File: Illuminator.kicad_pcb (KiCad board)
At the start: 2 copper layers, 70 x 70 mm, 14 parts, among them J0 Conn_01x03_Male, Q0 BSN20

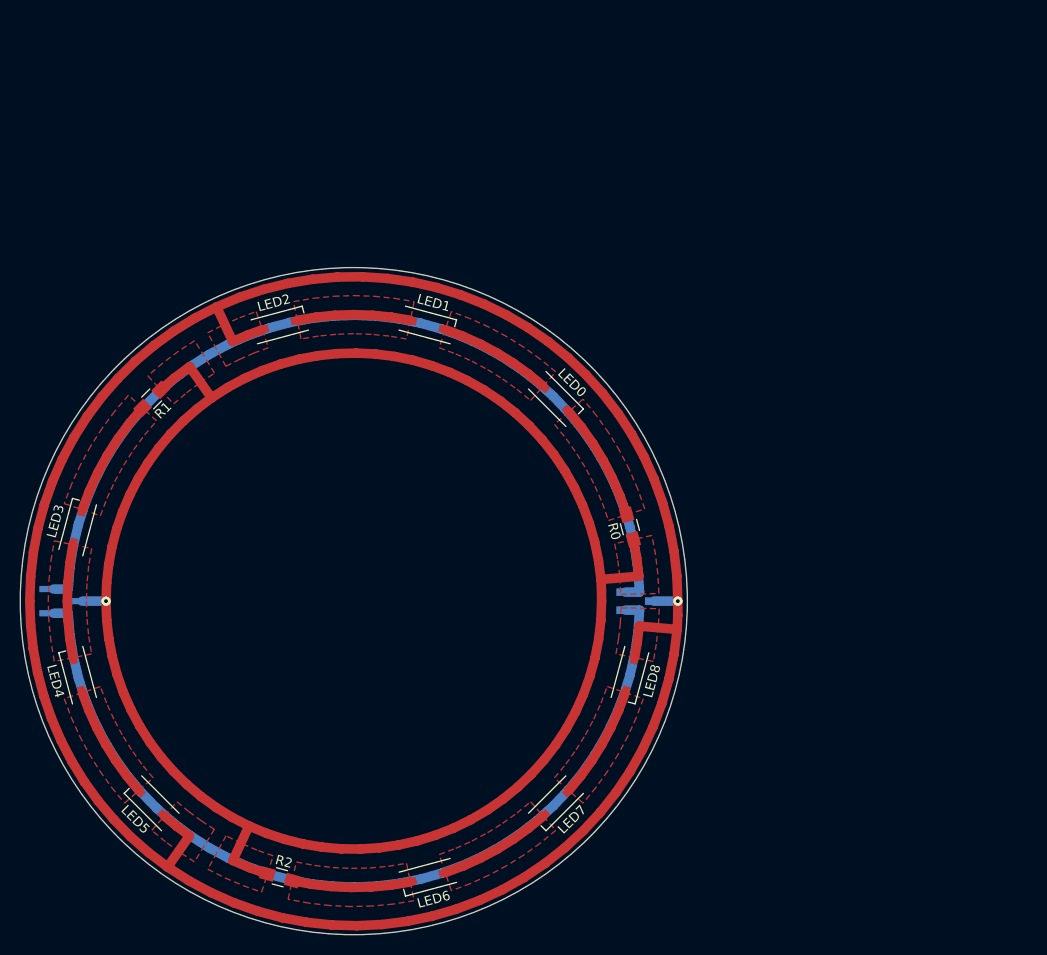
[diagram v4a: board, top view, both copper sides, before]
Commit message: Bugfixes in radial.py and resetting pcb
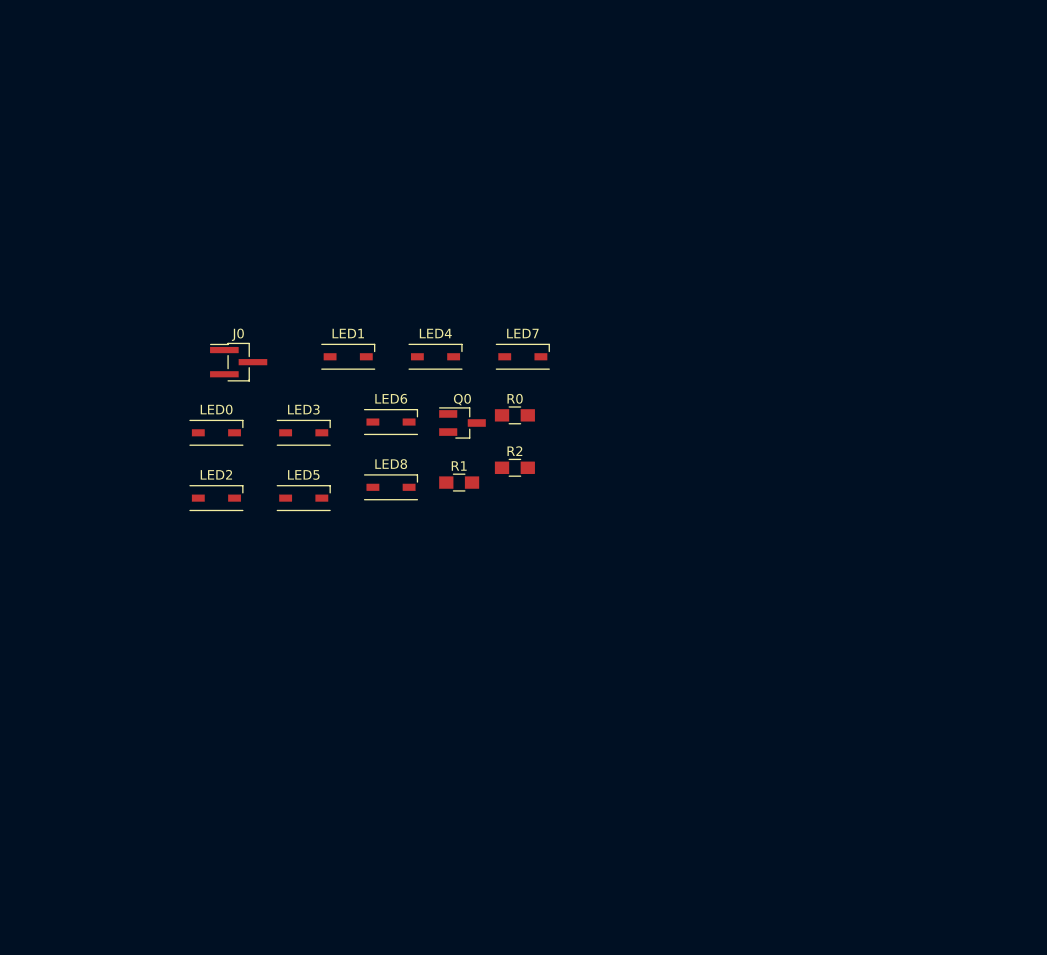
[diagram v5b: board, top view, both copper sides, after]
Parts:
- J0, Q0: moved to F.Cu
- moved LED4 50.3 mm to (108.6, 74.4), turned to 0 degrees
- moved R2 49.5 mm to (116.9, 86.0), turned to 0 degrees
- moved LED6 47.9 mm to (103.9, 81.2), turned to 0 degrees
- moved LED7 47.0 mm to (117.7, 74.4), turned to 0 degrees
- moved LED0 35.8 mm to (85.6, 82.3), turned to 0 degrees
- moved LED5 35.8 mm to (94.7, 89.2), turned to 0 degrees
- moved R1 33.4 mm to (111.1, 87.6), turned to 0 degrees
- moved LED8 31.9 mm to (103.9, 88.1), turned to 0 degrees
- moved J0 30.8 mm to (87.9, 74.9)
- moved Q0 26.4 mm to (111.4, 81.3)
- moved LED3 25.7 mm to (94.7, 82.3), turned to 0 degrees
- moved LED2 19.3 mm to (85.6, 89.2), turned to 0 degrees
- moved R0 16.8 mm to (116.9, 80.5), turned to 0 degrees
- moved LED1 8.99 mm to (99.4, 74.4), turned to 0 degrees
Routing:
- net Net-(LED2-Pad1): track 238.4 -> 0.00 mm, vias 1 -> 0
- net /TO_5V: track 189.6 -> 0.00 mm, vias 1 -> 0
- net /TO_GND: track 95.0 -> 0.00 mm
- net /TO_3V3: track 95.0 -> 0.00 mm
- net Net-(LED3-Pad2): track 12.5 -> 0.00 mm
- net Net-(LED6-Pad2): track 12.5 -> 0.00 mm
- net Net-(LED0-Pad2): track 12.5 -> 0.00 mm
- net Net-(LED3-Pad1): track 11.9 -> 0.00 mm
- net Net-(LED1-Pad1): track 11.9 -> 0.00 mm
- net Net-(LED4-Pad1): track 11.9 -> 0.00 mm
- net Net-(LED6-Pad1): track 11.9 -> 0.00 mm
- net Net-(LED7-Pad1): track 11.9 -> 0.00 mm
- net Net-(LED0-Pad1): track 11.9 -> 0.00 mm
- removed copper zone on F.Cu, net /TO_5V
- removed copper zone on F.Cu, net Net-(LED0-Pad1)
- removed copper zone on F.Cu, net Net-(LED0-Pad2)
- removed copper zone on F.Cu, net Net-(LED1-Pad1)
- removed copper zone on F.Cu, net Net-(LED2-Pad1)
- removed copper zone on F.Cu, net Net-(LED3-Pad1)
- removed copper zone on F.Cu, net Net-(LED3-Pad2)
- removed copper zone on F.Cu, net Net-(LED4-Pad1)
- removed copper zone on F.Cu, net Net-(LED6-Pad1)
- removed copper zone on F.Cu, net Net-(LED6-Pad2)
- removed copper zone on F.Cu, net Net-(LED7-Pad1)
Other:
- board outline removed

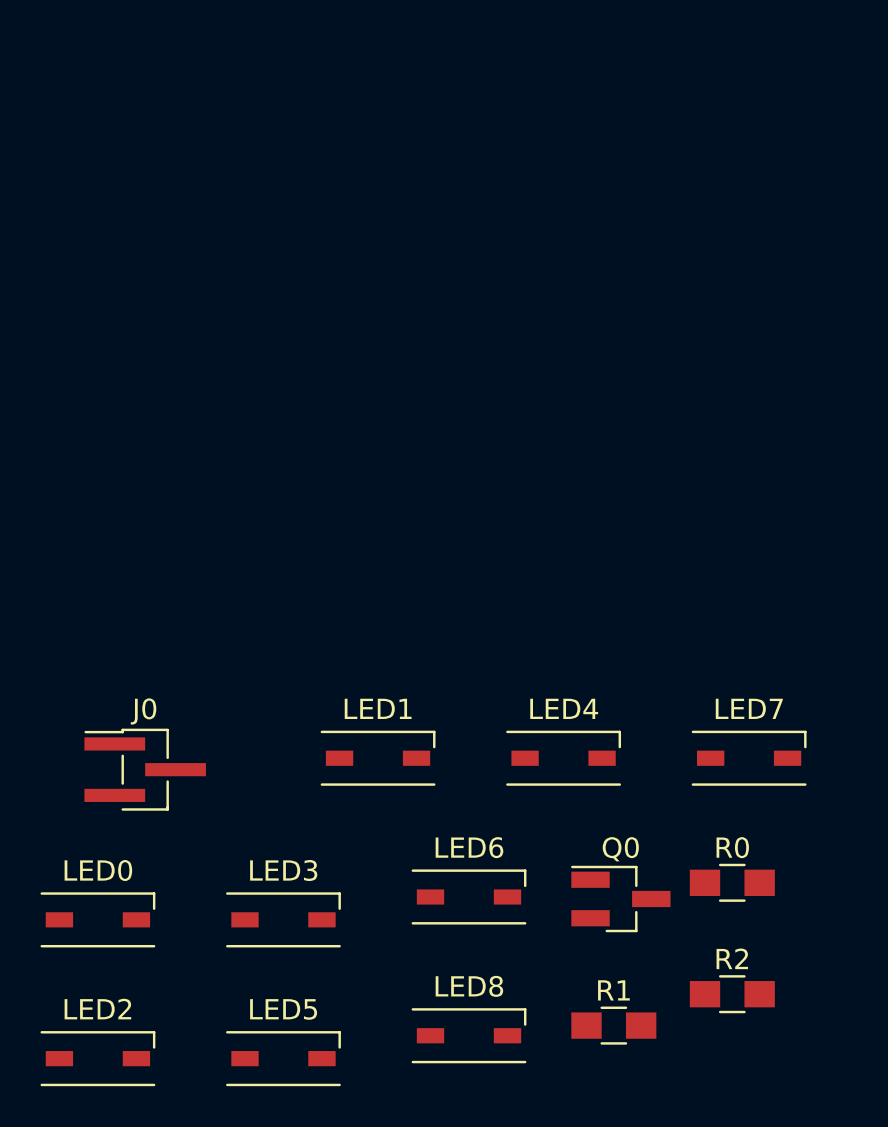
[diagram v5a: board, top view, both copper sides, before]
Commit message: Adding circular drawing for debug
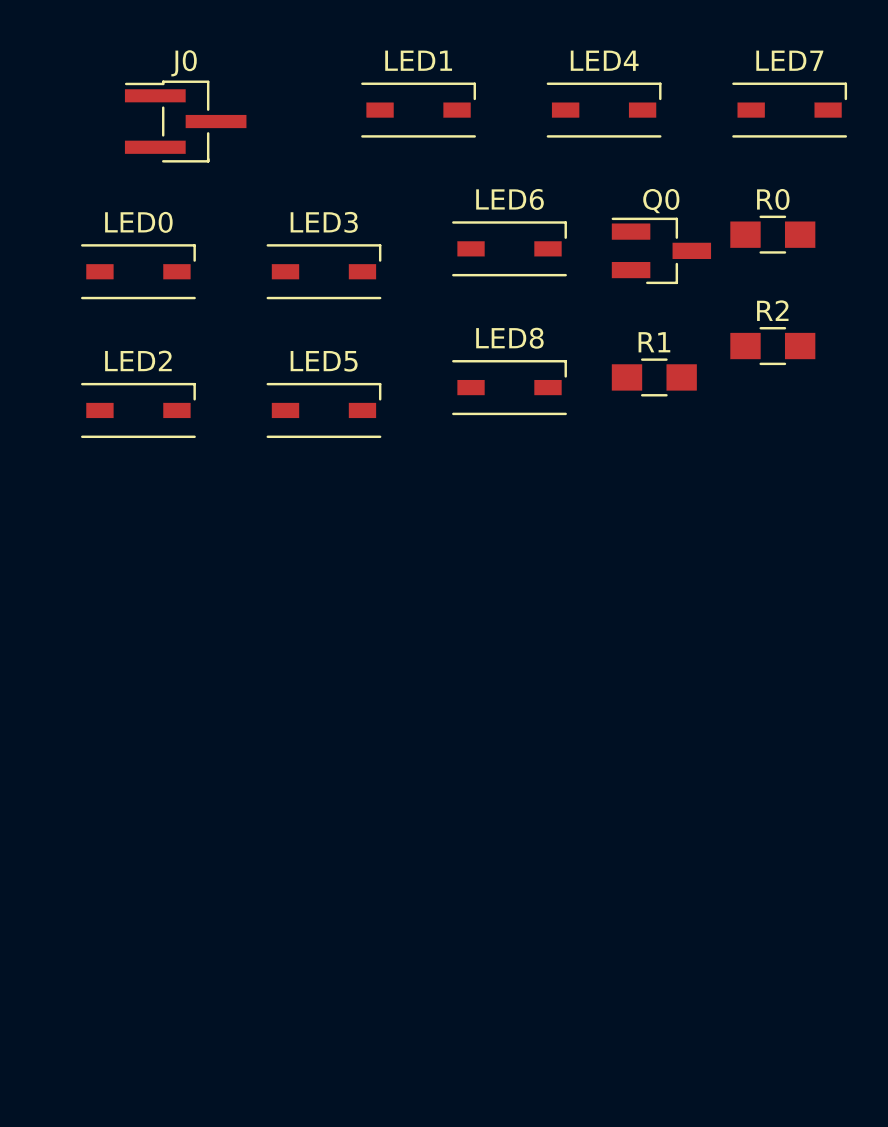
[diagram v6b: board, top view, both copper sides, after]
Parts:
- moved LED0 32.1 mm to (87.6, 50.3)
- moved LED3 32.1 mm to (96.7, 50.3)
- moved LED8 32.1 mm to (105.9, 56.1)
- moved Q0 32.1 mm to (113.4, 49.3)
- moved R1 32.1 mm to (113.1, 55.6)
- moved J0 32.1 mm to (89.9, 42.9)
- moved LED1 32.1 mm to (101.4, 42.4)
- moved LED2 32.1 mm to (87.6, 57.2)
- moved LED4 32.1 mm to (110.6, 42.4)
- moved LED5 32.1 mm to (96.7, 57.2)
- moved LED7 32.1 mm to (119.7, 42.4)
- moved LED6 32.1 mm to (105.9, 49.2)
- moved R0 32.1 mm to (118.9, 48.5)
- moved R2 32.1 mm to (118.9, 54.0)
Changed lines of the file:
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@@
 (general
   (thickness 1.6)
-  (drawings 0)
+  (drawings 1)
   (tracks 0)
   (zones 0)
@@
 (general
   (thickness 1.6)
-  (drawings 0)
+  (drawings 1)
   (tracks 0)
   (zones 0)
@@
 )
   (module Pin_Headers:Pin_Header_Straight_1x03_Pitch1.27mm_SMD_Pin1Left (layer F.Cu)
-    (at 87.917857 74.9225)
+    (at 89.917857 42.9225)
     (descr "surface-mounted straight pin header, 1x03, 1.27mm pitch, single row, style 1 (pin 1 left)")
     (tags "Surface mounted pin header SMD 1x03 1.27mm single row style1 pin1 left")
@@
   )
   (module Ratcam:LED-GW_2.3x2.3mm (layer F.Cu)
-    (at 85.584524 82.3375)
+    (at 87.584524 50.3375)
     (descr "2.0mm x 2.0mm PLCC4 LED, http://www.cree.com/~/media/Files/Cree/LED-Components-and-Modules/HB/Data-Sheets/CLMVBFKA.pdf")
     (tags "LED Cree PLCC-4")
@@
   )
   (module Ratcam:LED-GW_2.3x2.3mm (layer F.Cu)
-    (at 99.414524 74.3575)
+    (at 101.414524 42.3575)
     (descr "2.0mm x 2.0mm PLCC4 LED, http://www.cree.com/~/media/Files/Cree/LED-Components-and-Modules/HB/Data-Sheets/CLMVBFKA.pdf")
     (tags "LED Cree PLCC-4")
@@
   )
   (module Ratcam:LED-GW_2.3x2.3mm (layer F.Cu)
-    (at 85.584524 89.1875)
+    (at 87.584524 57.1875)
     (descr "2.0mm x 2.0mm PLCC4 LED, http://www.cree.com/~/media/Files/Cree/LED-Components-and-Modules/HB/Data-Sheets/CLMVBFKA.pdf")
     (tags "LED Cree PLCC-4")
@@
   )
   (module Ratcam:LED-GW_2.3x2.3mm (layer F.Cu)
-    (at 94.744524 82.3375)
+    (at 96.744524 50.3375)
     (descr "2.0mm x 2.0mm PLCC4 LED, http://www.cree.com/~/media/Files/Cree/LED-Components-and-Modules/HB/Data-Sheets/CLMVBFKA.pdf")
     (tags "LED Cree PLCC-4")
@@
   )
   (module Ratcam:LED-GW_2.3x2.3mm (layer F.Cu)
-    (at 108.574524 74.3575)
+    (at 110.574524 42.3575)
     (descr "2.0mm x 2.0mm PLCC4 LED, http://www.cree.com/~/media/Files/Cree/LED-Components-and-Modules/HB/Data-Sheets/CLMVBFKA.pdf")
     (tags "LED Cree PLCC-4")
@@
   )
   (module Ratcam:LED-GW_2.3x2.3mm (layer F.Cu)
-    (at 94.744524 89.1875)
+    (at 96.744524 57.1875)
     (descr "2.0mm x 2.0mm PLCC4 LED, http://www.cree.com/~/media/Files/Cree/LED-Components-and-Modules/HB/Data-Sheets/CLMVBFKA.pdf")
     (tags "LED Cree PLCC-4")
@@
   )
   (module Ratcam:LED-GW_2.3x2.3mm (layer F.Cu)
-    (at 103.904524 81.2075)
+    (at 105.904524 49.2075)
     (descr "2.0mm x 2.0mm PLCC4 LED, http://www.cree.com/~/media/Files/Cree/LED-Components-and-Modules/HB/Data-Sheets/CLMVBFKA.pdf")
     (tags "LED Cree PLCC-4")
@@
   )
   (module Ratcam:LED-GW_2.3x2.3mm (layer F.Cu)
-    (at 117.734524 74.3575)
+    (at 119.734524 42.3575)
     (descr "2.0mm x 2.0mm PLCC4 LED, http://www.cree.com/~/media/Files/Cree/LED-Components-and-Modules/HB/Data-Sheets/CLMVBFKA.pdf")
     (tags "LED Cree PLCC-4")
@@
   )
   (module Ratcam:LED-GW_2.3x2.3mm (layer F.Cu)
-    (at 103.904524 88.0575)
+    (at 105.904524 56.0575)
     (descr "2.0mm x 2.0mm PLCC4 LED, http://www.cree.com/~/media/Files/Cree/LED-Components-and-Modules/HB/Data-Sheets/CLMVBFKA.pdf")
     (tags "LED Cree PLCC-4")
@@
   )
   (module TO_SOT_Packages_SMD:SOT-23_Handsoldering (layer F.Cu)
-    (at 111.405001 81.3075)
+    (at 113.405001 49.3075)
     (descr "SOT-23, Handsoldering")
     (tags SOT-23)
@@
   )
   (module Resistors_SMD:R_0805_HandSoldering (layer F.Cu)
-    (at 116.905001 80.5075)
+    (at 118.905001 48.5075)
     (descr "Resistor SMD 0805, hand soldering")
     (tags "resistor 0805")
@@
   )
   (module Resistors_SMD:R_0805_HandSoldering (layer F.Cu)
-    (at 111.055001 87.5575)
+    (at 113.055001 55.5575)
     (descr "Resistor SMD 0805, hand soldering")
     (tags "resistor 0805")
@@
   )
   (module Resistors_SMD:R_0805_HandSoldering (layer F.Cu)
-    (at 116.905001 86.0075)
+    (at 118.905001 54.0075)
     (descr "Resistor SMD 0805, hand soldering")
     (tags "resistor 0805")
@@
     )
   )
+  (gr_circle (center 100 100) (end 130 100) (layer Dwgs.User) (width 0.2))
 )

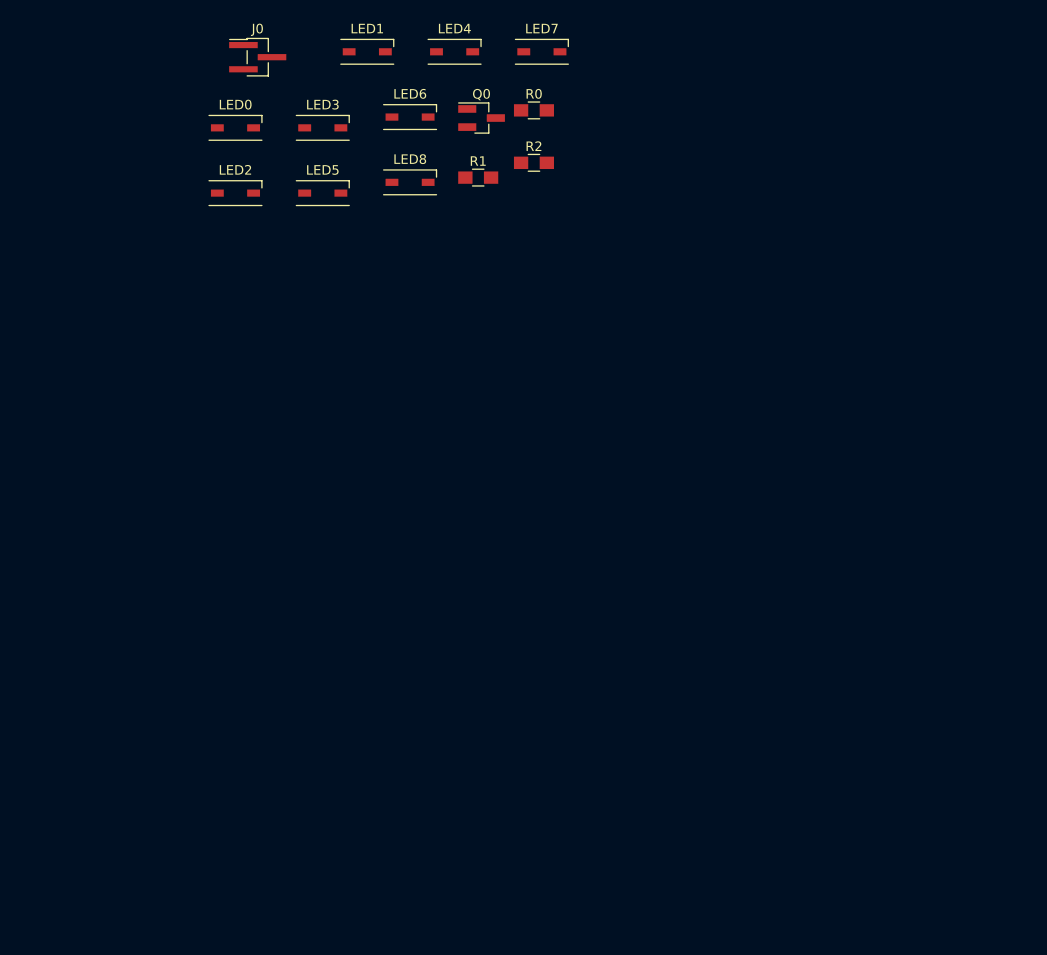
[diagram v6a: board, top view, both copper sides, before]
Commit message: Resetting the layout from the new netlist
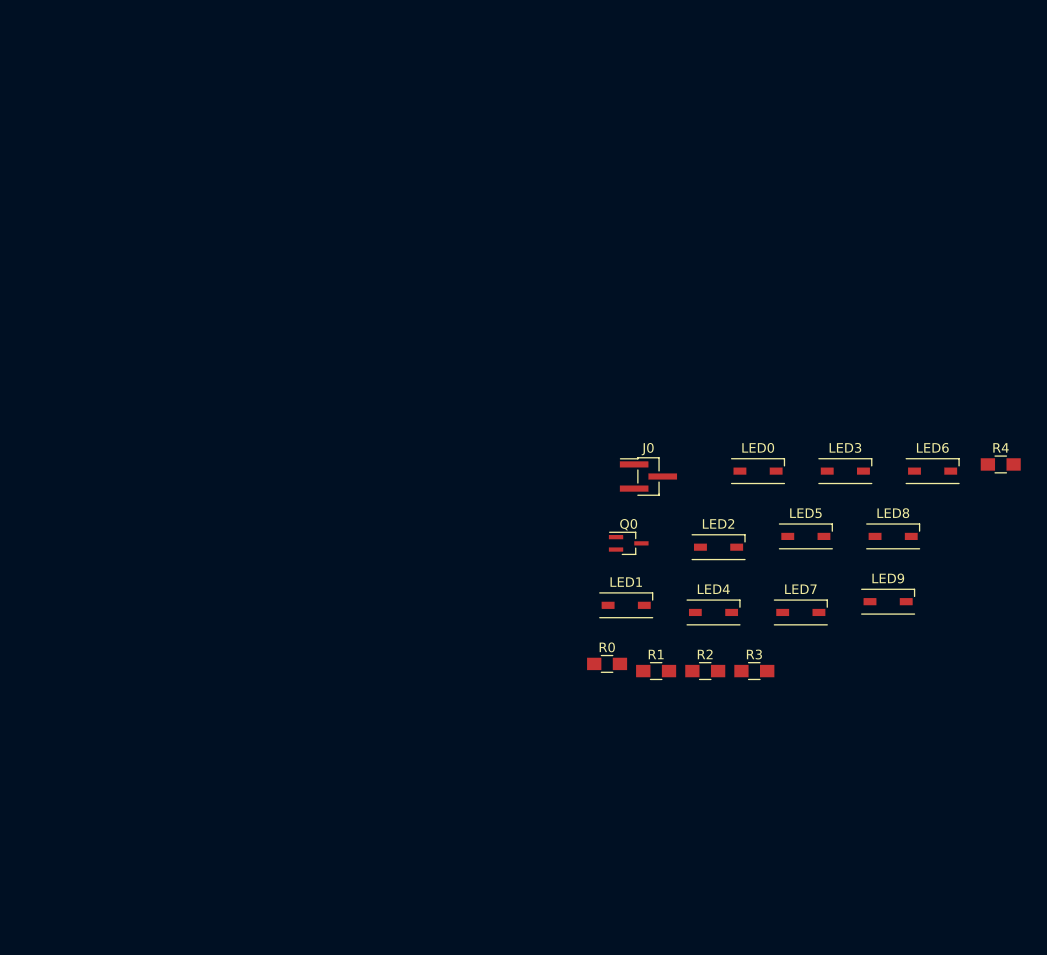
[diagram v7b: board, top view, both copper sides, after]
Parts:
- added LED9: VSMY2850G, Ratcam:LED-GW_2.3x2.3mm, F.Cu at (156.1, 100.1)
- added R3: 15, Resistors_SMD:R_0805_HandSoldering, F.Cu at (142.0, 107.3)
- added R4: 15, Resistors_SMD:R_0805_HandSoldering, F.Cu at (167.9, 85.7)
- Q0: value BSN20 -> DMG1012UW; footprint TO_SOT_Packages_SMD:SOT-23_Handsoldering -> TO_SOT_Packages_SMD:SOT-323_SC-70_Handsoldering
- R0, R1, R2: value 4.75 -> 15
- moved LED6 66.2 mm to (160.7, 86.4)
- moved LED0 65.6 mm to (142.4, 86.4)
- moved LED3 65.6 mm to (151.6, 86.4)
- moved LED4 64.8 mm to (137.7, 101.2)
- moved LED7 64.8 mm to (146.9, 101.2)
- moved LED1 64.1 mm to (128.6, 100.4)
- moved LED2 62.8 mm to (138.3, 94.3)
- moved LED8 62.8 mm to (156.6, 93.2)
- moved LED5 62.2 mm to (147.4, 93.2)
- moved J0 60.1 mm to (130.9, 86.9)
- moved R0 58.6 mm to (126.6, 106.6)
- moved R2 56.3 mm to (136.9, 107.3)
- moved R1 55.0 mm to (131.7, 107.3)
- moved Q0 47.2 mm to (128.8, 93.9)
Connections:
- LED2 pad 2: Net-(LED1-Pad1) -> Net-(LED2-Pad2)
- LED3 pad 1: Net-(LED3-Pad1) -> Net-(LED1-Pad1)
- LED3 pad 2: Net-(LED3-Pad2) -> Net-(LED2-Pad1)
- LED4 pad 2: Net-(LED3-Pad1) -> Net-(LED4-Pad2)
- LED5 pad 1: Net-(LED2-Pad1) -> Net-(LED1-Pad1)
- LED7 pad 1: Net-(LED7-Pad1) -> Net-(LED1-Pad1)
- LED8 pad 1: Net-(LED2-Pad1) -> Net-(LED8-Pad1)
- LED8 pad 2: Net-(LED7-Pad1) -> Net-(LED8-Pad2)
- Q0 pad 3: Net-(LED2-Pad1) -> Net-(LED1-Pad1)
- R1 pad 2: Net-(LED3-Pad2) -> Net-(LED2-Pad2)
- R2 pad 2: Net-(LED6-Pad2) -> Net-(LED4-Pad2)
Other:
- net class Default: trace_width 0.25 -> 1; via_dia 0.8 -> 1
- rule trace_min: 0.2 -> 1
- rule via_min_drill: 0.3 -> 0.4
- rule via_min_size: 0.4 -> 1
